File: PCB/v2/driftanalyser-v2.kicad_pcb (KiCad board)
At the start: 2 copper layers, 110 x 75 mm, 101 parts, among them J1 XT60PW-M, J11 LED1, J12 LED2, J13 LED3, J14 LED4, J15 LED5, J16 LED6, J2 USB-C 16P, J3 UART0, J4 EXT, J5 microSD, J6 OBD, SW1 EN, SW2 BOOT, U1 ESP32-S3-WROOM-1-N16R2, U2 BTS7002-1EPP, U3 AP63200WU-7, U4 AP7361C-33E, U5 LSM6DS3TR-C, U6 USBLC6-2SC6, U7 74HCT245PW, U8 TJA1051T/3, U9 TJA1027T/20

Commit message: pcb v2: placement tests, jlc drc minima, buck loop
Claude-Session: https://claude.ai/code/session_015oqRiQH5gUcw5a6jvR5Zdk
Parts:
- moved R4 18.8 mm to (51.0, 48.5)
- moved R3 13.5 mm to (51.0, 51.0)
- moved C11 8.10 mm to (59.3, 55.0)
- moved C10 7.50 mm to (47.5, 53.5)
- moved C9 6.86 mm to (46.8, 60.6), turned to 0 degrees
- moved L1 5.22 mm to (53.5, 57.0)
- moved C12 2.80 mm to (59.3, 58.5)

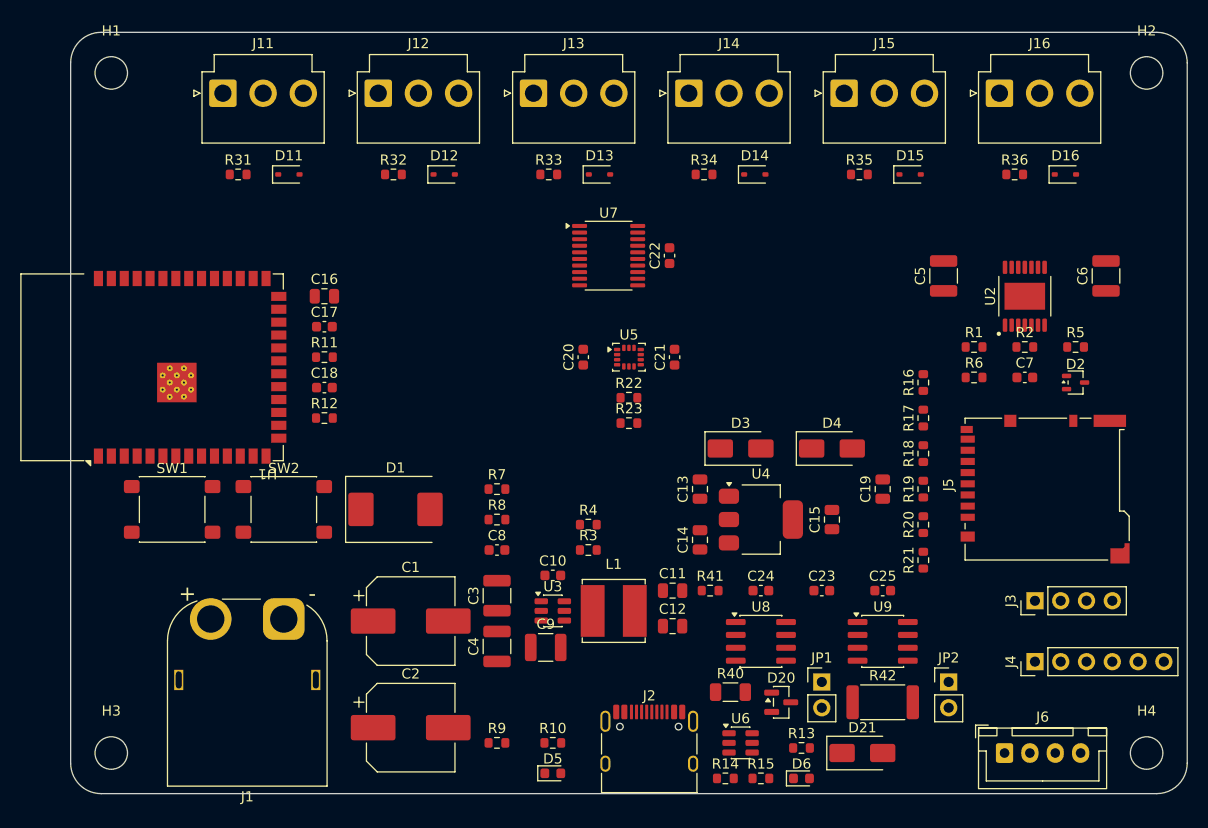
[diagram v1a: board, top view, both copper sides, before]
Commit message: pcb v2: power zones, stitching, drc clean except routing
Claude-Session: https://claude.ai/code/session_015oqRiQH5gUcw5a6jvR5Zdk
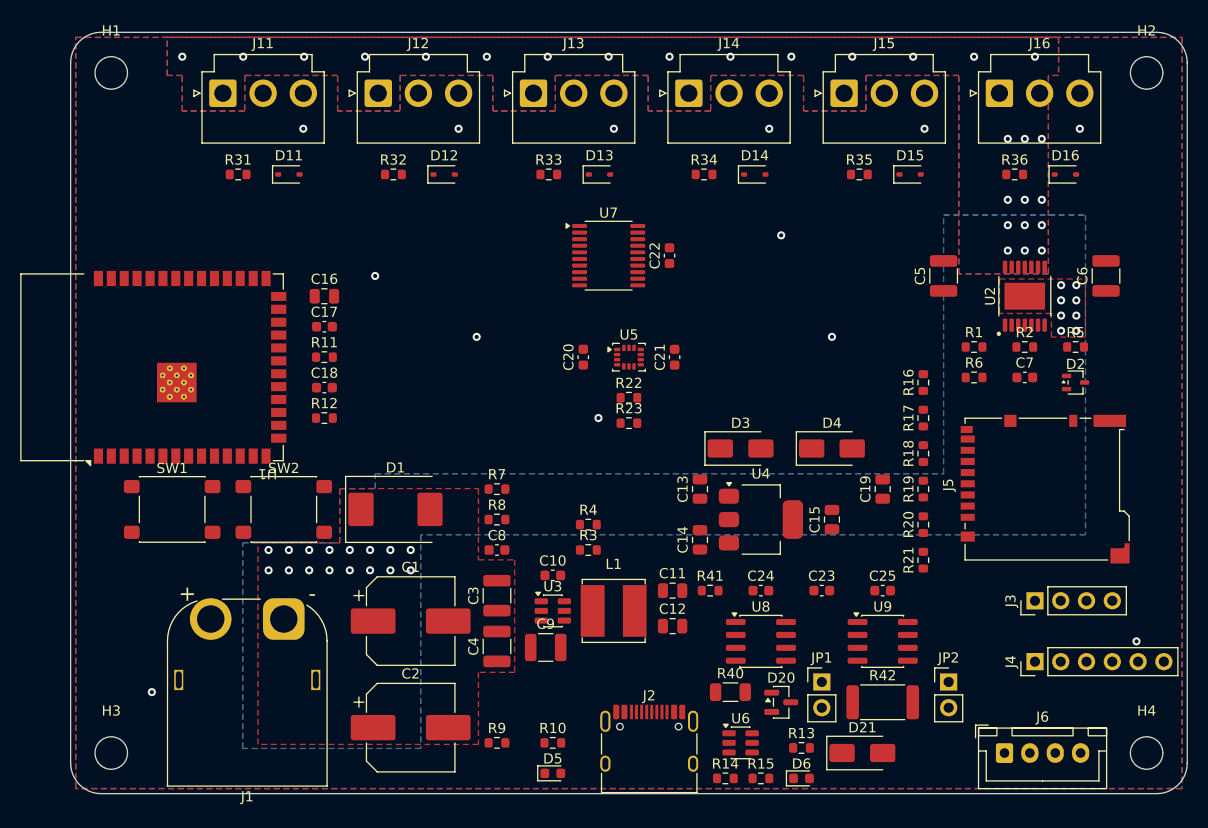
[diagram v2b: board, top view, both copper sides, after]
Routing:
- net VBAT: vias 0 -> 24
- net GND: vias 0 -> 13
- net 12V_LED: vias 0 -> 27
- added copper zone on B.Cu, net 12V_LED
- added copper zone on F.Cu, net 12V_LED
- added copper zone on B.Cu, net GND
- added copper zone on F.Cu, net GND
- added copper zone on B.Cu, net VBAT
- added copper zone on F.Cu, net VBAT
